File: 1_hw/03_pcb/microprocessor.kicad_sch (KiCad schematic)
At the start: 30 parts

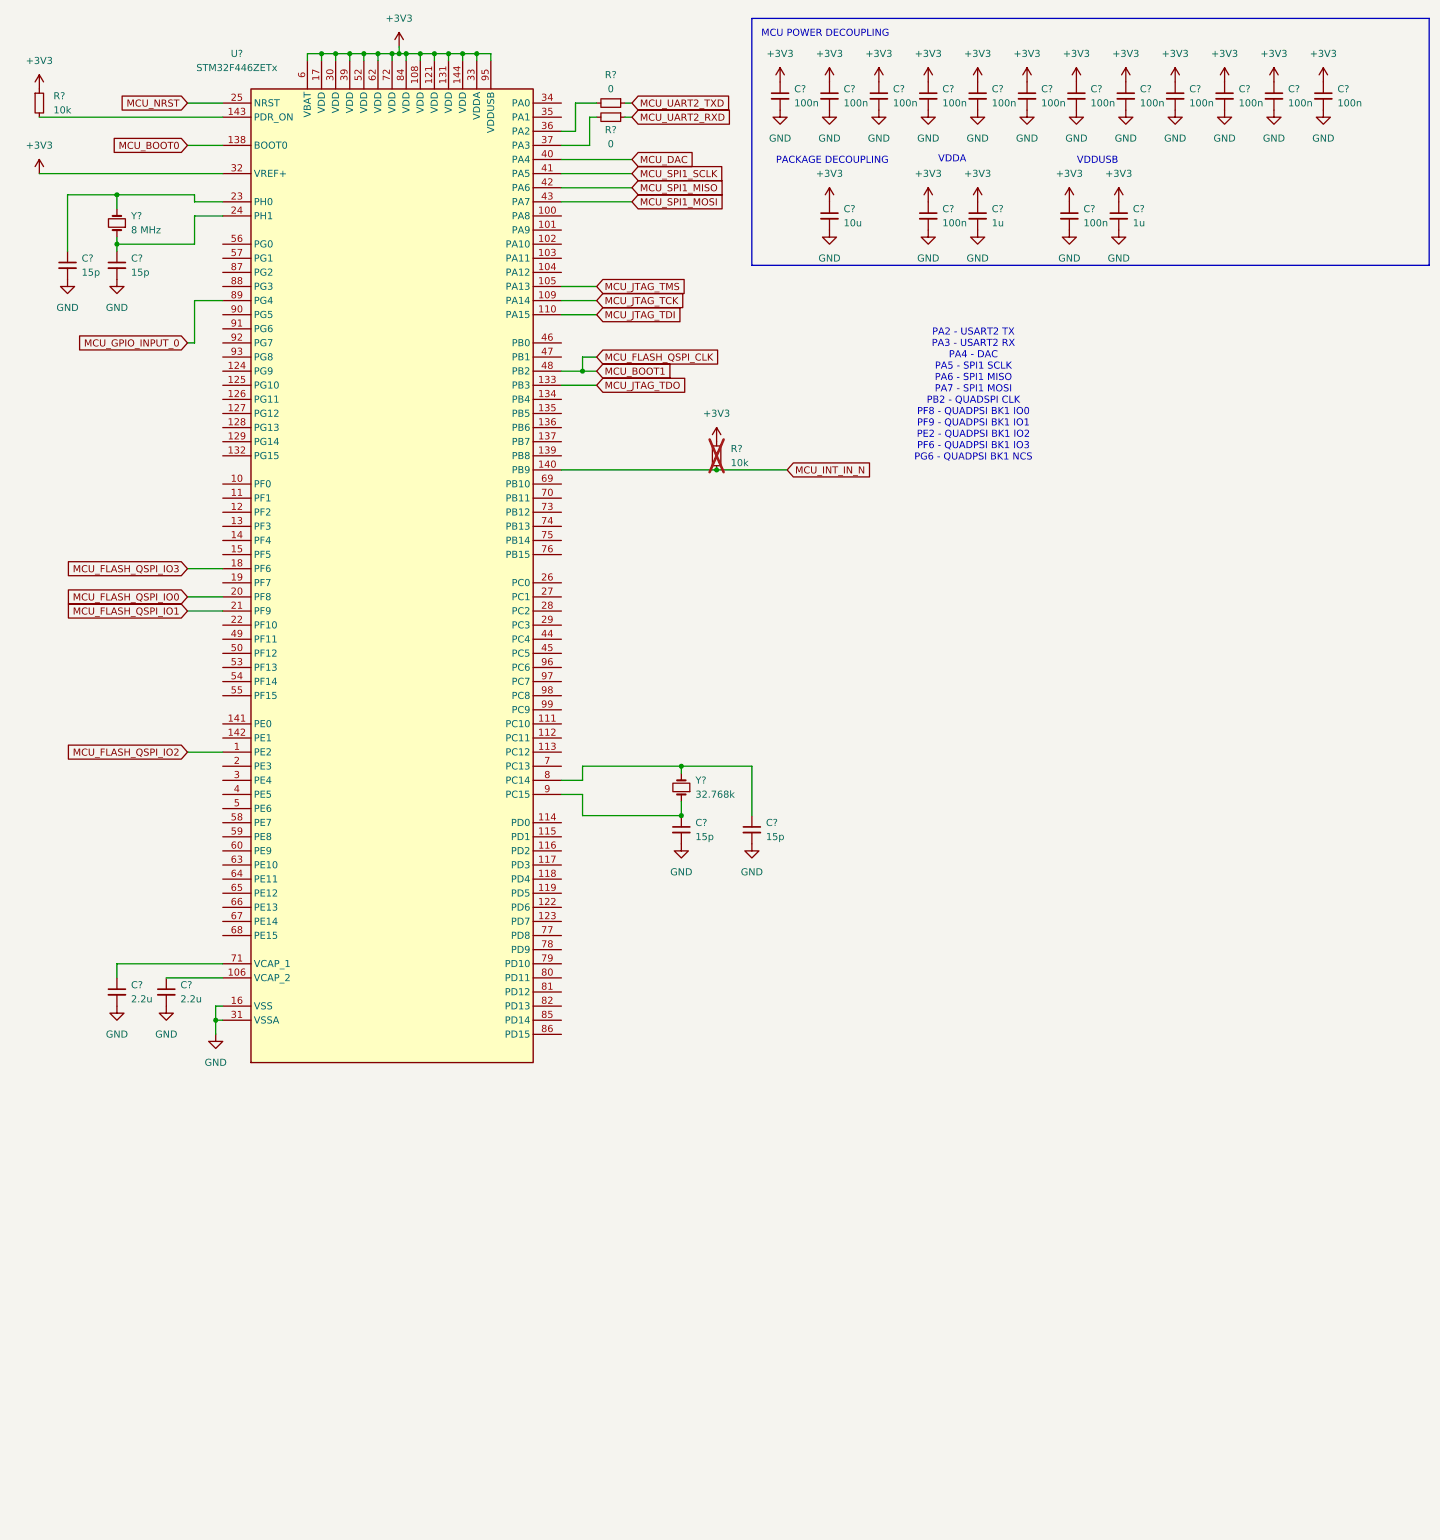
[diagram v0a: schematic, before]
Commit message: FEAT: Finished Excel Pin Map for MCU. Completed MCU + FPGA in Schematic.
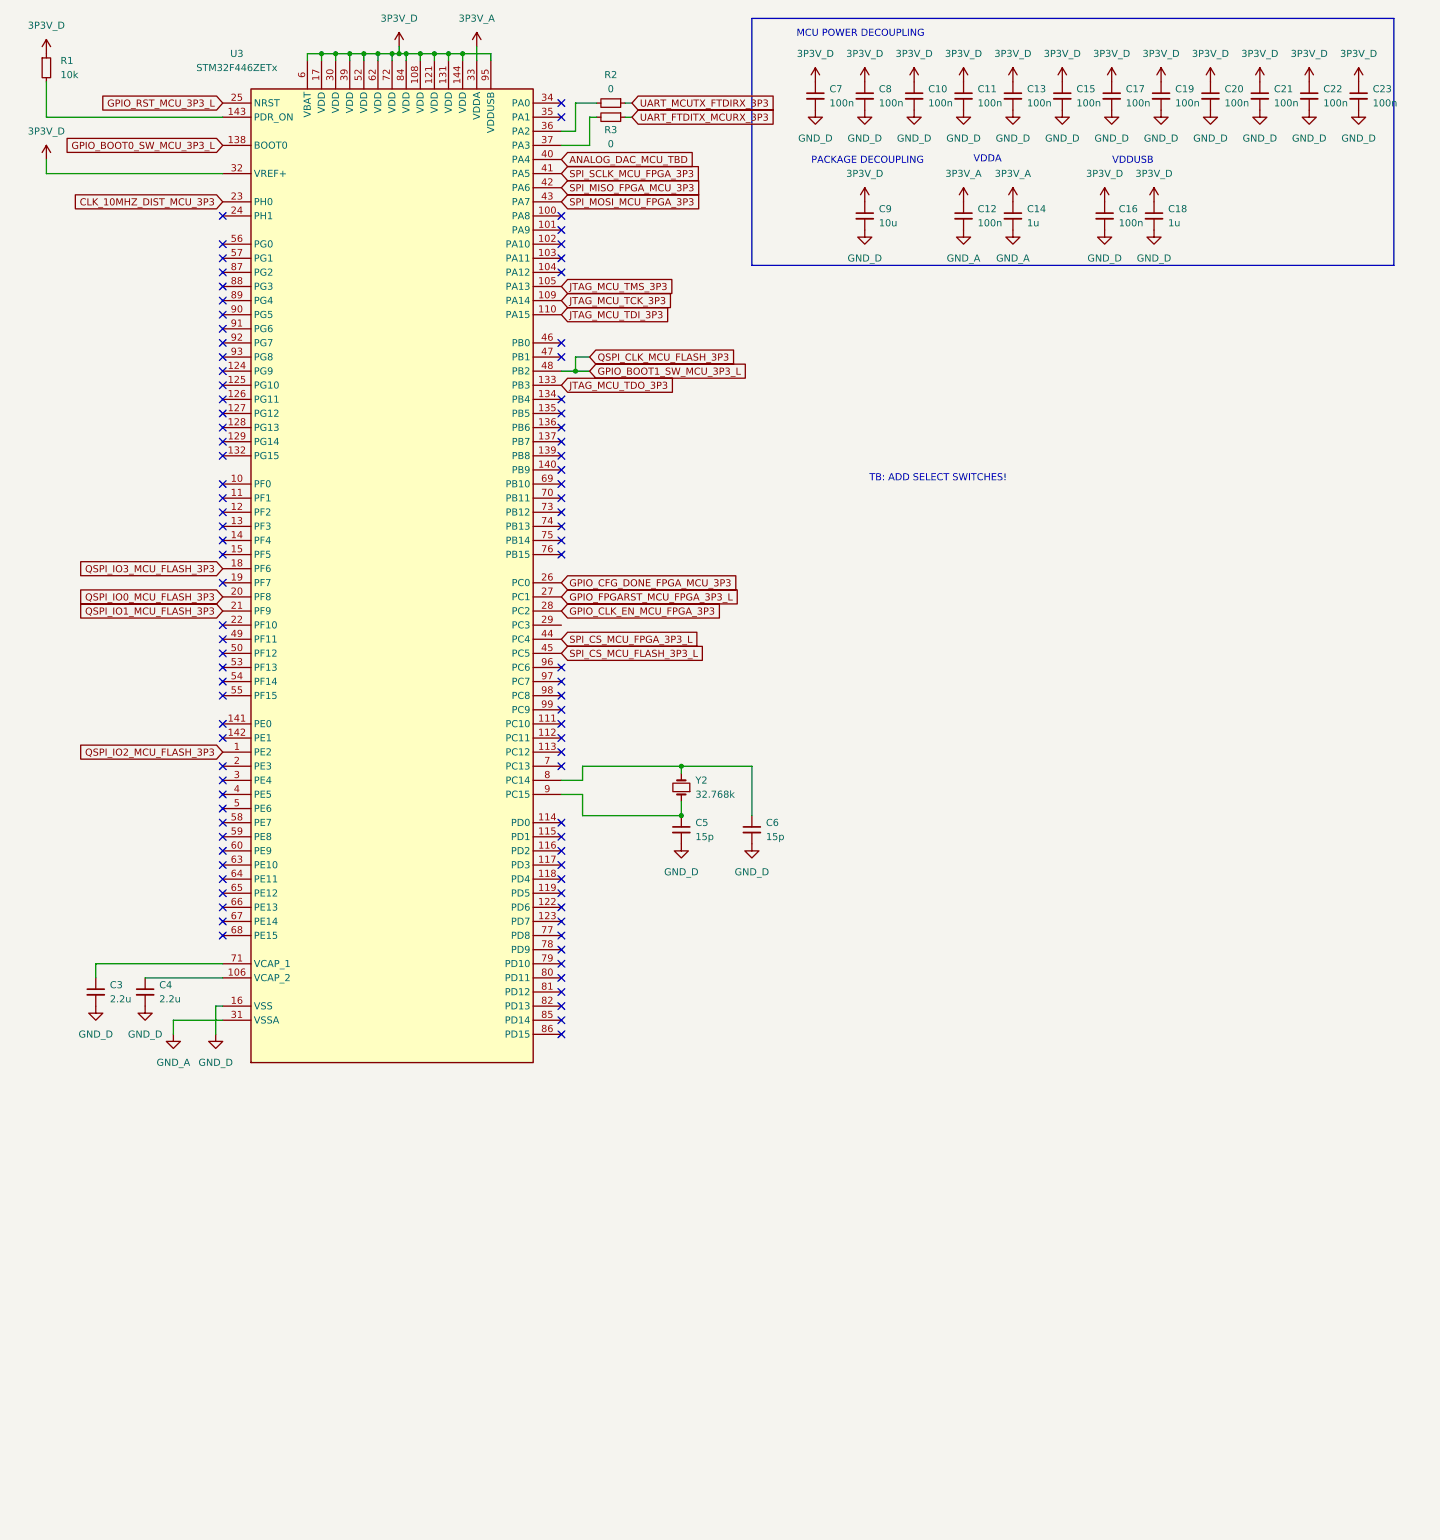
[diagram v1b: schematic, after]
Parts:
- removed C? (x2): 15p, Capacitor_SMD:C_0603_1608Metric, symbol Device:C_Small
- removed R?: 10k, Resistor_SMD:R_0603_1608Metric, symbol Device:R_Small
- removed Y?: 8 MHz, Crystal:Crystal_SMD_3225-4Pin_3.2x2.5mm, symbol Device:Crystal_Small
- gave numbers to parts that had none: 26
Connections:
- net CLK_10MHZ_DIST_MCU_3P3: now reaches U3.23 (PH0)
- net GPIO_CFG_DONE_FPGA_MCU_3P3: now reaches U3.26 (PC0)
- net GPIO_FPGARST_MCU_FPGA_3P3_L: now reaches U3.27 (PC1)
- net GPIO_CLK_EN_MCU_FPGA_3P3: now reaches U3.28 (PC2)
- net SPI_CS_MCU_FPGA_3P3_L: now reaches U3.44 (PC4)
- net SPI_CS_MCU_FLASH_3P3_L: now reaches U3.45 (PC5)
- net +3V3 renamed 3P3V_D
- net 3P3V_D: no longer C12.1, C14.1, U3.33 (VDDA)
- net GND renamed GND_D
- net GND_D: no longer C12.2, C14.2, U3.31 (VSSA)
- net MCU_BOOT0 renamed GPIO_BOOT0_SW_MCU_3P3_L
- net MCU_BOOT1 renamed GPIO_BOOT1_SW_MCU_3P3_L
- net MCU_DAC renamed ANALOG_DAC_MCU_TBD
- net MCU_FLASH_QSPI_IO0 renamed QSPI_IO0_MCU_FLASH_3P3
- net MCU_FLASH_QSPI_IO1 renamed QSPI_IO1_MCU_FLASH_3P3
- net MCU_FLASH_QSPI_IO2 renamed QSPI_IO2_MCU_FLASH_3P3
- net MCU_FLASH_QSPI_IO3 renamed QSPI_IO3_MCU_FLASH_3P3
- net MCU_GPIO_INPUT_0: no longer names the net of U3.89 (PG4)
- net MCU_INT_IN_N: no longer names the net of U3.140 (PB9)
- net MCU_JTAG_TCK renamed JTAG_MCU_TCK_3P3
- net MCU_JTAG_TDI renamed JTAG_MCU_TDI_3P3
- net MCU_JTAG_TDO renamed JTAG_MCU_TDO_3P3
- net MCU_JTAG_TMS renamed JTAG_MCU_TMS_3P3
- net MCU_NRST renamed GPIO_RST_MCU_3P3_L
- net MCU_SPI1_MISO renamed SPI_MISO_FPGA_MCU_3P3
- net MCU_SPI1_MOSI renamed SPI_MOSI_MCU_FPGA_3P3
- net MCU_SPI1_SCLK renamed SPI_SCLK_MCU_FPGA_3P3
- net MCU_UART2_RXD renamed UART_FTDITX_MCURX_3P3
- net MCU_UART2_TXD renamed UART_MCUTX_FTDIRX_3P3
- new net 3P3V_A: C12.1, C14.1, U3.33 (VDDA)
- new net GND_A: C12.2, C14.2, U3.31 (VSSA)
- no-connect marks 0 -> 90
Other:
- note added: "TB: ADD SELECT SWITCHES!"
- note removed: "PA2 - USART2 TX PA3 - USART2 RX PA4 - DAC PA5 - SPI1 SCLK PA6 - SPI1 MISO PA7 - SPI1 MOSI PB2 - QUADSPI CLK PF8 - QUADPSI BK1 IO0 PF9 - QUADPSI BK1 IO1 PE2 - QUADPSI BK1 IO2 PF6 - QUADPSI BK1 IO3 PG6 - QUADPSI BK1 NCS"
- moved on the sheet: C10, C11, C12, C13, C14, C15, C16, C17, C18, C19, C20, C21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

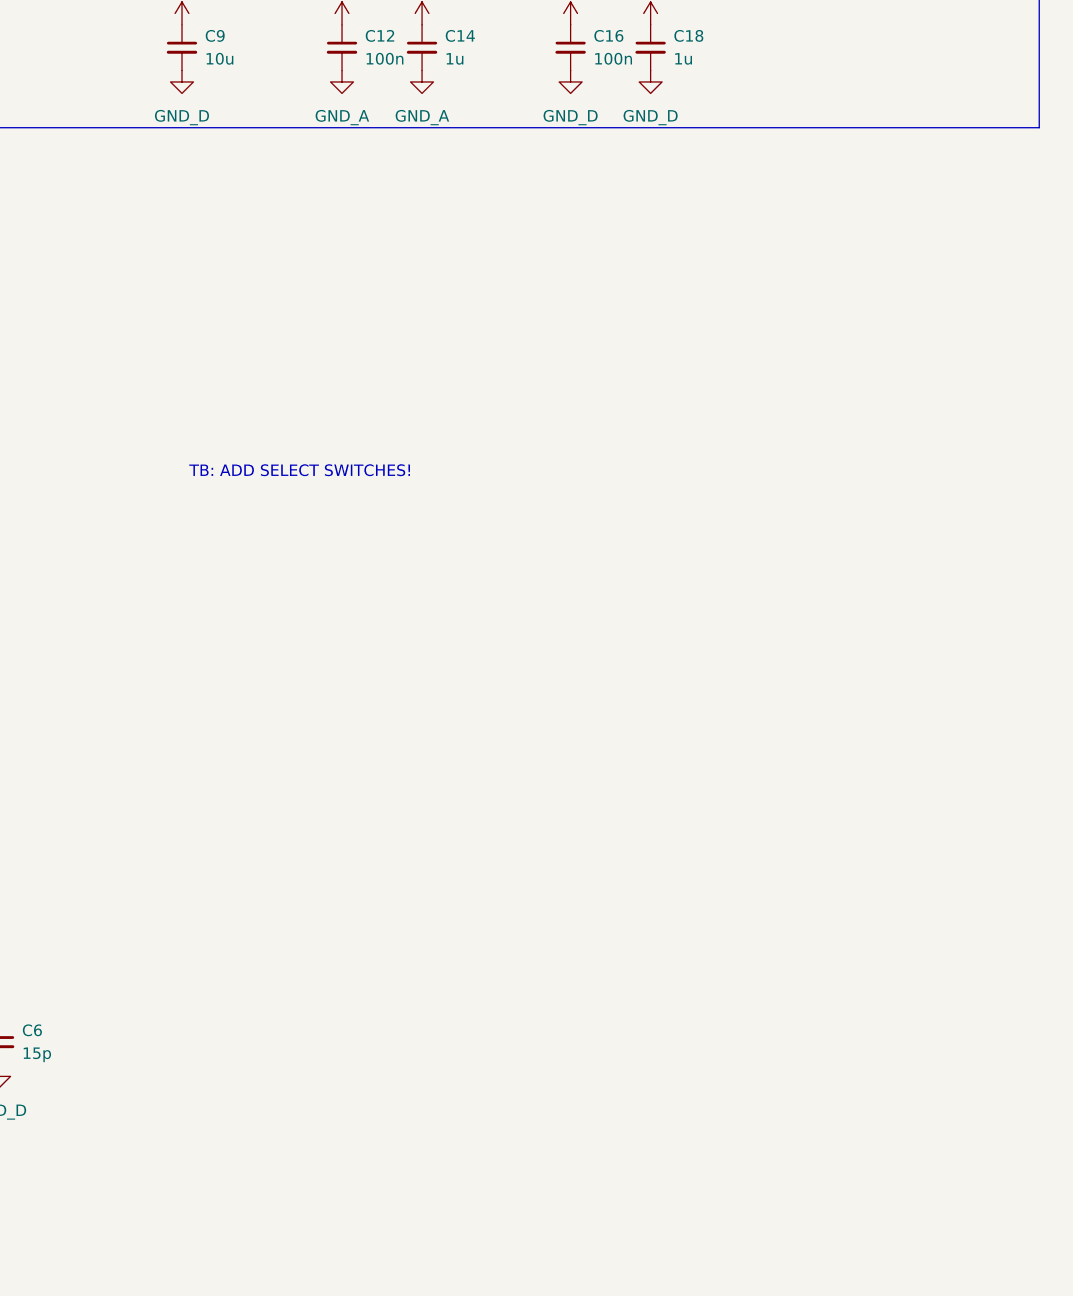
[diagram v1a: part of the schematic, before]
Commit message: FEAT: Added FTDI JTAG. Added 0 Ohm JTAG Resistors. Added Boot Select Switches.
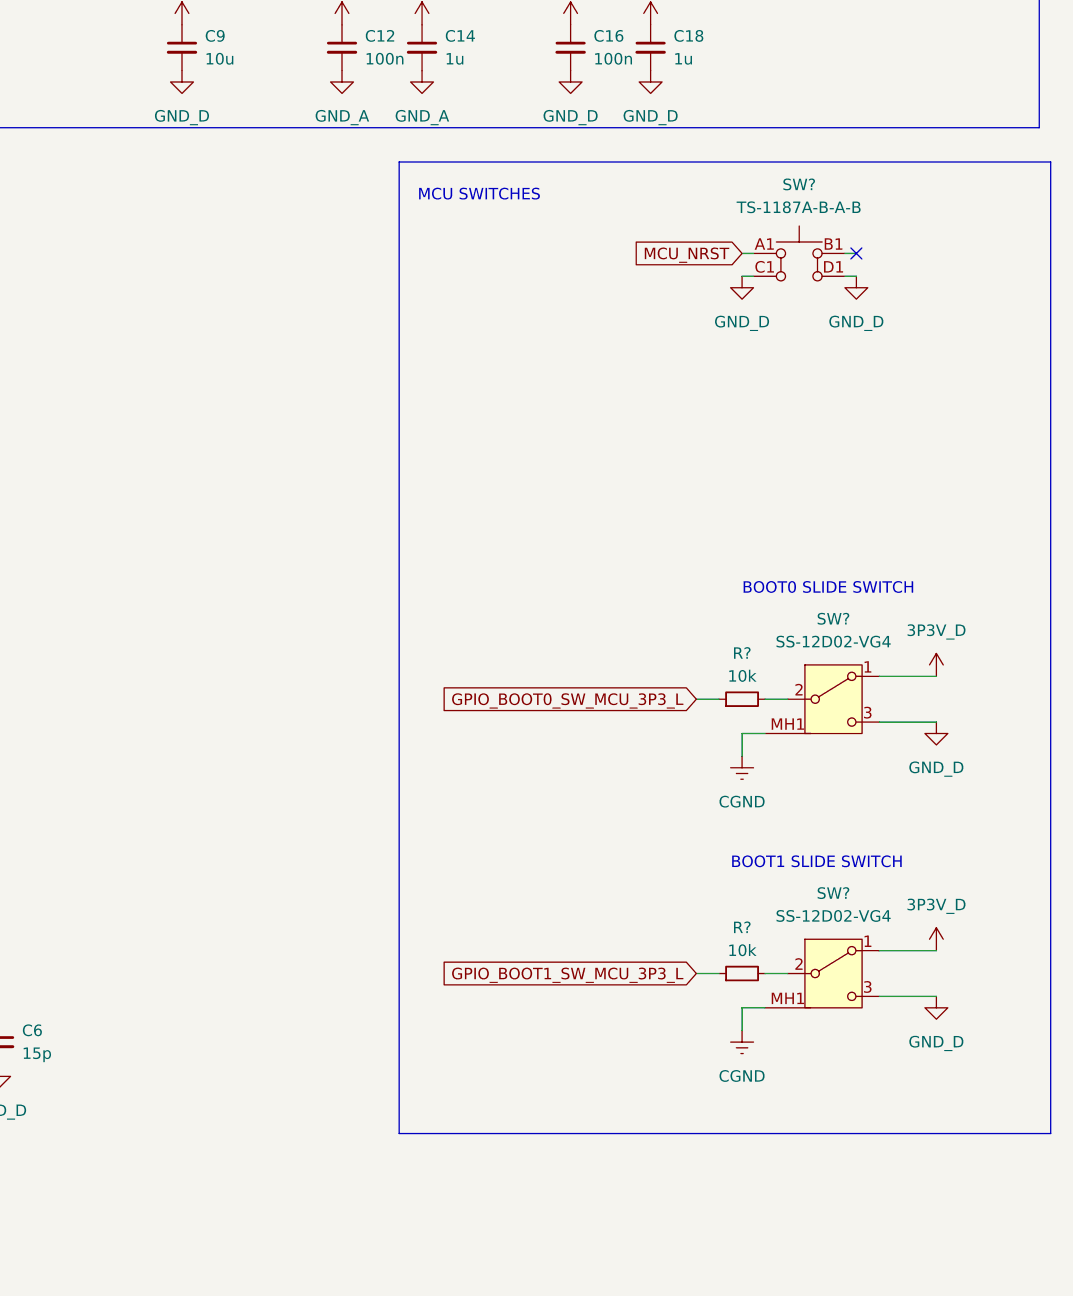
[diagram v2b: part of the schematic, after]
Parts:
- added R? (x2): 10k, Resistor_SMD:R_0603_1608Metric, symbol Device:R_Small
- added SW? (x2): SS-12D02-VG4, symbol BRZK_SWITCH:SS-12D02-VG4
- added SW?: TS-1187A-B-A-B, TS1187ABAB, symbol BRZK_SWITCH:TS-1187A-B-A-B
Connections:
- net 3P3V_D: now also SW?.1 (NC), SW?.1 (NC)
- net GND_D: now also SW?.3 (NO), SW?.3 (NO), SW?.C1 (NO_1), SW?.D1 (NO_2)
- net GPIO_BOOT0_SW_MCU_3P3_L: now also R?.1
- net GPIO_BOOT1_SW_MCU_3P3_L: now also R?.1
- new net: R?.2, SW?.2 (COM) (x2)
- new net CGND: SW?.MH1, SW?.MH1, SW?.MH2, SW?.MH2
- new net MCU_NRST: SW?.A1 (COM_1)
- no-connect marks 90 -> 91
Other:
- note added: "BOOT0 SLIDE SWITCH"
- note added: "BOOT1 SLIDE SWITCH"
- note added: "MCU SWITCHES"
- note removed: "TB: ADD SELECT SWITCHES!"
